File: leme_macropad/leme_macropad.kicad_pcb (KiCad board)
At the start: 4 copper layers, 99.9 x 63.9 mm, 95 parts, among them J1 USB_C_Receptacle_USB2.0_16P, J2 OLED display, SW1 SW_Push, SW10 SW_Push, SW2 SW_Push, SW3 SW_Push, SW4 SW_Push, SW5 SW_Push, SW6 SW_Push, SW7 RotaryEncoder_Switch, SW8 SW_Push, SW9 SW_Push, U1 SRV05-4HTG-D, U2 NCP1117-3.3_SOT223, U3 W25Q128JVS, U4 RP2040, Y1 ABM8-272-T3

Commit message: Moves switch on top layer to be hidden under the display
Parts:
- moved SW8 51.6 mm to (140.8, 74.2)
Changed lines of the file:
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@@
 		(locked yes)
 		(layer "F.Cu")
-		(at 171 116 90)
+		(at 140.75 74.19 90)
 		(descr "SMT SPST pushbutton")
 		(tags "button pushbutton SPST")

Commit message: Brings RP2040 and components around it closer to where they'll be
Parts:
- C1, C10, C11, C12, C13, C14, C15, C16, C17, C2, C3, C4, C5, C6, C7, C8, C9, R1, R10, R11, R2, R3, R4, R5, R6, R7, R8, R9, U1, U2, U3, U4, Y1: moved to B.Cu
- moved R11 193.6 mm to (195.2, 46.8), turned to 180 degrees
- moved R8 173.2 mm to (176.0, 46.8)
- moved C3 164.1 mm to (208.9, 79.0), turned to 180 degrees
- moved C5 164.1 mm to (208.9, 84.0), turned to 180 degrees
- moved R10 157.7 mm to (179.8, 106.7), turned to 90 degrees
- moved R9 156.2 mm to (179.8, 113.3), turned to -90 degrees
- moved C10 155.4 mm to (204.5, 84.0), turned to 180 degrees
- moved C11 155.4 mm to (204.5, 86.5), turned to 180 degrees
- moved C12 155.4 mm to (204.5, 89.0), turned to 180 degrees
- moved C8 155.4 mm to (204.5, 79.0), turned to 180 degrees
- moved C9 155.4 mm to (204.5, 81.5), turned to 180 degrees
- moved C4 149.1 mm to (191.6, 66.8), turned to 180 degrees
- moved C13 146.8 mm to (200.2, 79.0), turned to 180 degrees
- moved C14 146.8 mm to (200.2, 81.5), turned to 180 degrees
- moved C15 146.8 mm to (200.2, 84.0), turned to 180 degrees
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
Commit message: Moves mounting point H2
This should open more space for the layout of the microcontroller and
everything else, while also hiding the only visible mounting whole and
securing even more the rotary encoder.
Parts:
- moved H2 23.3 mm to (190.0, 96.0)
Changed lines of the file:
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@@
 		(locked yes)
 		(layer "F.Cu")
-		(at 180 75)
+		(at 190 96.05)
 		(descr "Mounting Hole 2.2mm, M2, generated by kicad-footprint-generator mountinghole.py")
 		(tags "mountinghole M2")

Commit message: Removes SW8
This button was there just to complete the matrix but we have no use for
it. It would only make things harder to organize.
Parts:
- removed D8: D_Small, Diode_SMD:D_SOD-123
- removed SW8: SW_Push, leme_macropad:CK_PTS636_SK43_SMTR_LFS
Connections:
- net Encoder S2 renamed Net-(D7-A)

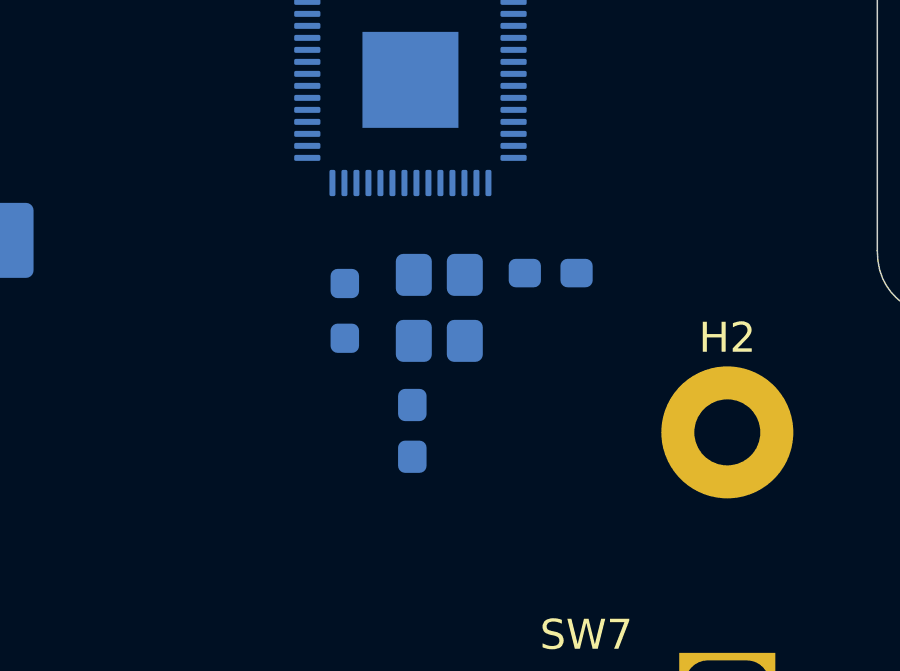
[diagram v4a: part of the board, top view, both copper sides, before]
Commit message: First draft of the layout for the crystal oscillator
This is not looking very good, but gives an idea of where the crystal
should be. This might also be a good indication that we need to change
the passives around the RP2040 to 0402, since 0603 are looking quite big
right now.
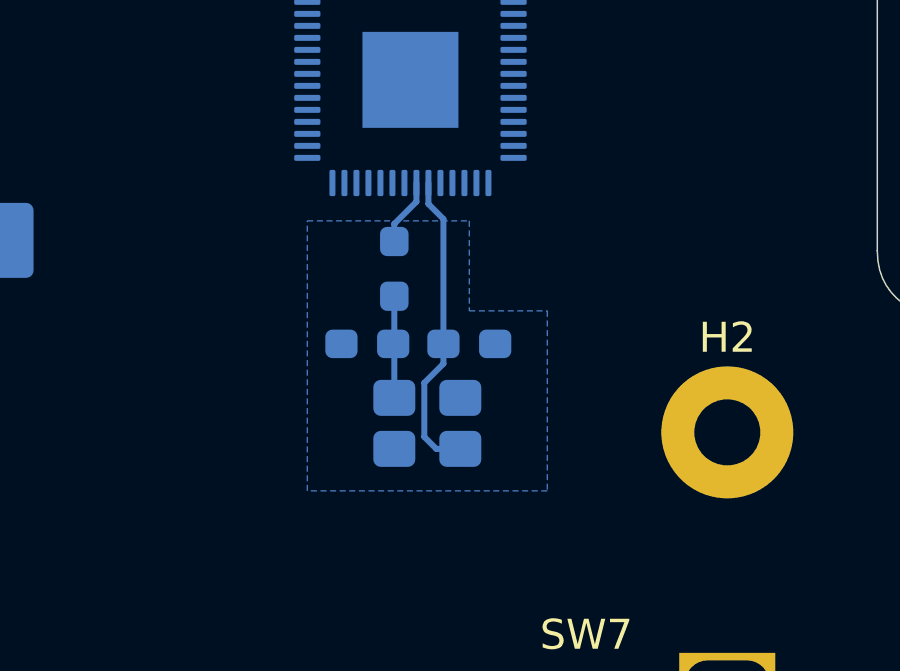
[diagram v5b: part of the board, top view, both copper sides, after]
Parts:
- moved Y1 3.87 mm to (180.0, 95.8), turned to 180 degrees
- moved C6 3.60 mm to (181.4, 93.1)
- moved C7 3.26 mm to (178.0, 93.1), turned to 0 degrees
- moved R3 2.16 mm to (178.9, 90.6)
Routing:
- net XIN: track 0.00 -> 10.3 mm
- net Net-(C7-Pad2): track 0.00 -> 3.42 mm
- net XOUT: track 0.00 -> 2.26 mm
- added copper zone on B.Cu, net GND
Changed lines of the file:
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@@
 	(footprint "Capacitor_SMD:C_0603_1608Metric_Pad1.08x0.95mm_HandSolder"
 		(layer "B.Cu")
-		(at 184.1125 90.74 180)
+		(at 181.4 93.1 180)
 		(descr "Capacitor SMD 0603 (1608 Metric), square (rectangular) end terminal, IPC-7351 nominal with elongated pad for handsoldering. (Body size source: IPC-SM-782 page 76, https://www.pcb-3d.com/wordpress/wp-content/uploads/ipc-sm-782a_amendment_1_and_2.pdf), generated with kicad-footprint-generator")
 		(tags "capacitor handsolder")
@@
 	(footprint "Resistor_SMD:R_0603_1608Metric_Pad0.98x0.95mm_HandSolder"
 		(layer "B.Cu")
-		(at 177.25 92 90)
+		(at 178.9 90.6 90)
 		(descr "Resistor SMD 0603 (1608 Metric), square (rectangular) end terminal, IPC-7351 nominal with elongated pad for handsoldering. (Body size source: IPC-SM-782 page 72, https://www.pcb-3d.com/wordpress/wp-content/uploads/ipc-sm-782a_amendment_1_and_2.pdf), generated with kicad-footprint-generator")
 		(tags "resistor handsolder")
@@
 	(footprint "Crystal:Crystal_SMD_3225-4Pin_3.2x2.5mm"
 		(layer "B.Cu")
-		(at 180.4 91.9 -90)
+		(at 180 95.75 180)
 		(descr "SMD3225/4, Crystal, 3.2x2.5mm package, SMD, generated with kicad-footprint-generator make_crystal.py, http://www.txccrystal.com/images/pdf/7m-accuracy.pdf")
 		(property "Reference" "Y1"
-			(at 0 2.45 90)
+			(at 0 2.45 0)
 			(layer "B.SilkS")
 			(effects
@@
 		)
 		(property "Value" "ABM8-272-T3"
-			(at 0 -2.45 90)
+			(at 0 -2.45 0)
 			(layer "B.Fab")
 			(effects
@@
 		)
 		(property "Datasheet" ""
-			(at 0 0 90)
+			(at 0 0 0)
 			(layer "B.Fab")
 			(hide yes)
@@
 		)
 		(property "Description" "Four pin crystal, GND on pins 2 and 4"
-			(at 0 0 90)
+			(at 0 0 0)
 			(layer "B.Fab")
 			(hide yes)
@@
 		)
 		(fp_text user "${REFERENCE}"
-			(at 0 0 90)
+			(at 0 0 0)
 			(layer "B.Fab")
 			(effects
@@
 		)
 		(pad "1" smd roundrect
-			(at -1.1 -0.85 270)
+			(at -1.1 -0.85 180)
 			(size 1.4 1.2)
 			(layers "B.Cu" "B.Mask" "B.Paste")
@@
 		)
 		(pad "2" smd roundrect
-			(at 1.1 -0.85 270)
+			(at 1.1 -0.85 180)
 			(size 1.4 1.2)
 			(layers "B.Cu" "B.Mask" "B.Paste")
@@
 		)
 		(pad "3" smd roundrect
-			(at 1.1 0.85 270)
+			(at 1.1 0.85 180)
 			(size 1.4 1.2)
 			(layers "B.Cu" "B.Mask" "B.Paste")
@@
 		)
 		(pad "4" smd roundrect
-			(at -1.1 0.85 270)
+			(at -1.1 0.85 180)
 			(size 1.4 1.2)
 			(layers "B.Cu" "B.Mask" "B.Paste")
@@
 	(footprint "Capacitor_SMD:C_0603_1608Metric_Pad1.08x0.95mm_HandSolder"
 		(layer "B.Cu")
-		(at 179.5 96 90)
+		(at 178 93.1)
 		(descr "Capacitor SMD 0603 (1608 Metric), square (rectangular) end terminal, IPC-7351 nominal with elongated pad for handsoldering. (Body size source: IPC-SM-782 page 76, https://www.pcb-3d.com/wordpress/wp-content/uploads/ipc-sm-782a_amendment_1_and_2.pdf), generated with kicad-footprint-generator")
 		(tags "capacitor handsolder")
 		(property "Reference" "C7"
-			(at 0 1.43 90)
+			(at 0 1.43 0)
 			(layer "B.SilkS")
 			(effects
@@
 		)
 		(property "Value" "15pF"
-			(at 0 -1.43 90)
+			(at 0 -1.43 0)
 			(layer "B.Fab")
 			(effects
@@
 		)
 		(property "Datasheet" ""
-			(at 0 0 90)
+			(at 0 0 0)
 			(layer "B.Fab")
 			(hide yes)
@@
 		)
 		(property "Description" "Unpolarized capacitor, small symbol"
-			(at 0 0 90)
+			(at 0 0 0)
 			(layer "B.Fab")
 			(hide yes)
@@
 		)
 		(fp_line
-			(start 1.65 -0.73)
-			(end -1.65 -0.73)
+			(start -1.65 -0.73)
+			(end -1.65 0.73)
 			(stroke
 				(width 0.05)
@@
 		)
 		(fp_line
-			(start -1.65 -0.73)
-			(end -1.65 0.73)
+			(start -1.65 0.73)
+			(end 1.65 0.73)
 			(stroke
 				(width 0.05)
@@
 		)
 		(fp_line
-			(start 1.65 0.73)
-			(end 1.65 -0.73)
+			(start 1.65 -0.73)
+			(end -1.65 -0.73)
 			(stroke
 				(width 0.05)
@@
 		)
 		(fp_line
-			(start -1.65 0.73)
-			(end 1.65 0.73)
+			(start 1.65 0.73)
+			(end 1.65 -0.73)
 			(stroke
 				(width 0.05)
@@
 		)
 		(fp_line
-			(start 0.8 -0.4)
-			(end -0.8 -0.4)
+			(start -0.8 -0.4)
+			(end -0.8 0.4)
 			(stroke
 				(width 0.1)
@@
 		)
 		(fp_line
-			(start -0.8 -0.4)
-			(end -0.8 0.4)
+			(start -0.8 0.4)
+			(end 0.8 0.4)
 			(stroke
 				(width 0.1)
@@
 		)
 		(fp_line
-			(start 0.8 0.4)
-			(end 0.8 -0.4)
+			(start 0.8 -0.4)
+			(end -0.8 -0.4)
 			(stroke
 				(width 0.1)
@@
 		)
 		(fp_line
-			(start -0.8 0.4)
-			(end 0.8 0.4)
+			(start 0.8 0.4)
+			(end 0.8 -0.4)
 			(stroke
 				(width 0.1)
@@
 		)
 		(fp_text user "${REFERENCE}"
-			(at 0 0 90)
+			(at 0 0 0)
 			(layer "B.Fab")
 			(effects
@@
 		)
 		(pad "1" smd roundrect
-			(at -0.8625 0 90)
+			(at -0.8625 0)
 			(size 1.075 0.95)
 			(layers "B.Cu" "B.Mask" "B.Paste")
@@
 		)
 		(pad "2" smd roundrect
-			(at 0.8625 0 90)
+			(at 0.8625 0)
 			(size 1.075 0.95)
 			(layers "B.Cu" "B.Mask" "B.Paste")
@@
 		)
 	)
+	(segment
+		(start 180.0375 87.7375)
+		(end 180.0375 88.4375)
+		(width 0.2)
+		(layer "B.Cu")
+		(net 4)
+	)
+	(segment
+		(start 180.5375 88.9375)
+		(end 180.5375 93.1)
+		(width 0.2)
+		(layer "B.Cu")
+		(net 4)
+	)
+	(segment
+		(start 179.9 96.2)
+		(end 180.3 96.6)
+		(width 0.2)
+		(layer "B.Cu")
+		(net 4)
+	)
+	(segment
+		(start 180.0375 88.4375)
+		(end 180.5375 88.9375)
+		(width 0.2)
+		(layer "B.Cu")
+		(net 4)
+	)
+	(segment
+		(start 180.5375 93.7625)
+		(end 179.9 94.4)
+		(width 0.2)
+		(layer "B.Cu")
+		(net 4)
+	)
+	(segment
+		(start 180.3 96.6)
+		(end 181.1 96.6)
+		(width 0.2)
+		(layer "B.Cu")
+		(net 4)
+	)
+	(segment
+		(start 180.5375 93.1)
+		(end 180.5375 93.7625)
+		(width 0.2)
+		(layer "B.Cu")
+		(net 4)
+	)
+	(segment
+		(start 179.9 94.4)
+		(end 179.9 96.2)
+		(width 0.2)
+		(layer "B.Cu")
+		(net 4)
+	)
+	(segment
+		(start 178.9 94.9)
+		(end 178.9 93.1375)
+		(width 0.2)
+		(layer "B.Cu")
+		(net 5)
+	)
+	(segment
+		(start 178.9 91.5125)
+		(end 178.9 93.0625)
+		(width 0.2)
+		(layer "B.Cu")
+		(net 5)
+	)
+	(segment
+		(start 178.9 93.0625)
+		(end 178.8625 93.1)
+		(width 0.2)
+		(layer "B.Cu")
+		(net 5)
+	)
+	(segment
+		(start 178.9 93.1375)
+		(end 178.8625 93.1)
+		(width 0.2)
+		(layer "B.Cu")
+		(net 5)
+	)
+	(segment
+		(start 178.9 89.1)
+		(end 179.6375 88.3625)
+		(width 0.2)
+		(layer "B.Cu")
+		(net 33)
+	)
+	(segment
+		(start 179.6375 88.3625)
+		(end 179.6375 87.7375)
+		(width 0.2)
+		(layer "B.Cu")
+		(net 33)
+	)
+	(segment
+		(start 178.9 89.6875)
+		(end 178.9 89.1)
+		(width 0.2)
+		(layer "B.Cu")
+		(net 33)
+	)
+	(zone
+		(net 2)
+		(net_name "GND")
+		(layer "B.Cu")
+		(hatch edge 0.5)
+		(connect_pads
+			(clearance 0.5)
+		)
+		(min_thickness 0.25)
+		(filled_areas_thickness no)
+		(fill yes
+			(thermal_gap 0.5)
+			(thermal_bridge_width 0.5)
+		)
+		(polygon
+			(pts
+				(xy 176 89) (xy 181.4 89) (xy 181.4 92) (xy 184 92) (xy 184 98) (xy 176 98)
+			)
+		)
+	)

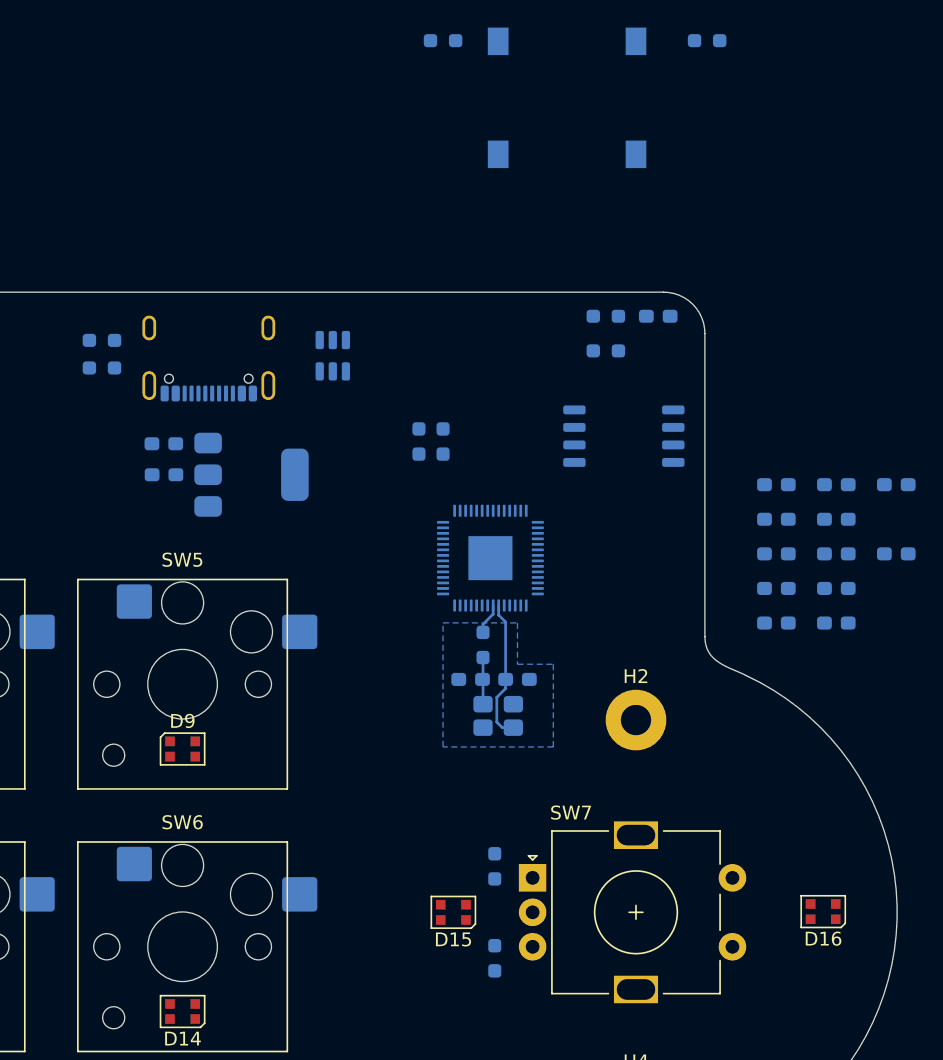
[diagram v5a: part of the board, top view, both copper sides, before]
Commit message: Changes resistors and capacitors to 0402
This should make it much easier to route things and to comply with the
signal integrity needs of some parts of the circuit.
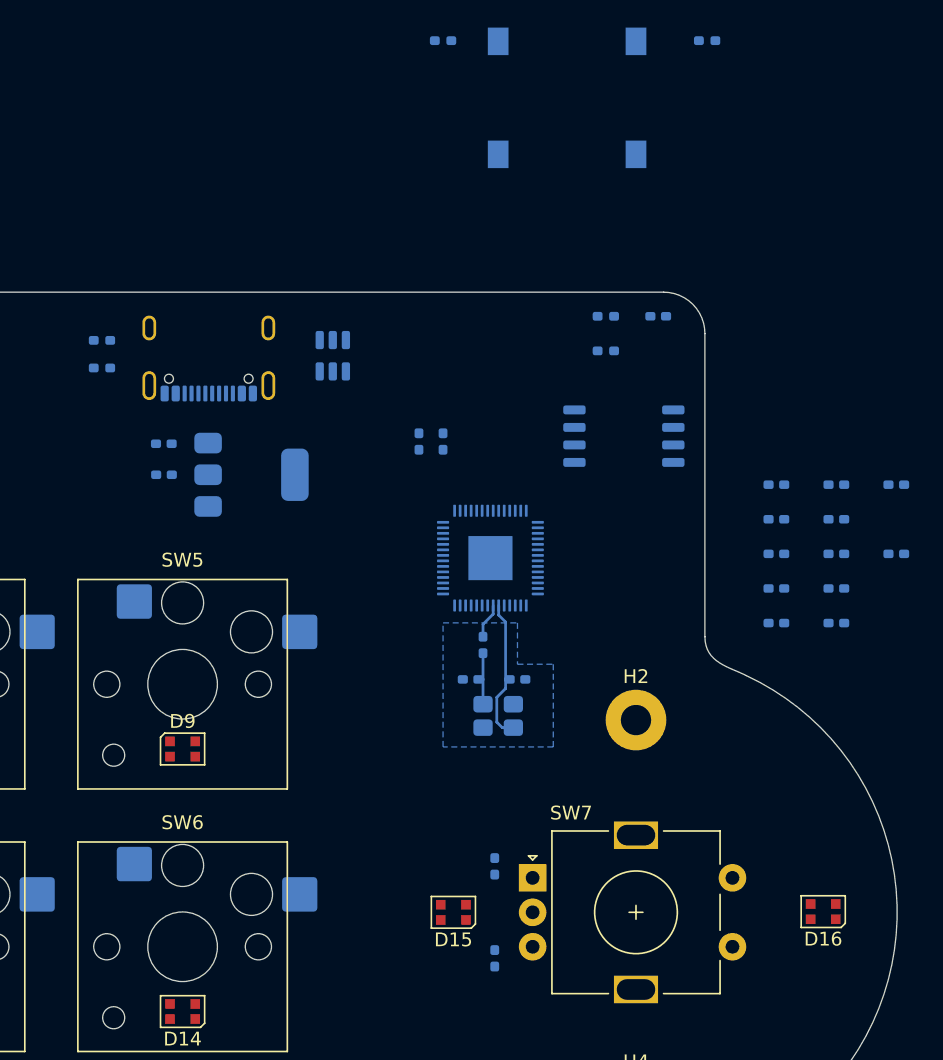
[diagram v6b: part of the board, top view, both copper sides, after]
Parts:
- C1, C10, C11, C12, C13, C14, C15, C16, C17, C2, C3, C4, C5, C6, C7, C8, C9: footprint Capacitor_SMD:C_0603_1608Metric_Pad1.08x0.95mm_HandSolder -> Capacitor_SMD:C_0402_1005Metric_Pad0.74x0.62mm_HandSolder
- R1, R10, R11, R2, R3, R4, R5, R6, R7, R8, R9: footprint Resistor_SMD:R_0603_1608Metric_Pad0.98x0.95mm_HandSolder -> Resistor_SMD:R_0402_1005Metric_Pad0.72x0.64mm_HandSolder
